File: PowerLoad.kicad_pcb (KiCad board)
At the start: 2 copper layers, 213.9 x 120 mm, 88 parts, among them IC1 L7812, J1 IN+, J2 IN-, J3 LOAD_IN+, J4 GND, J5 LOAD_IN+, U2 LM324, U3 LM324

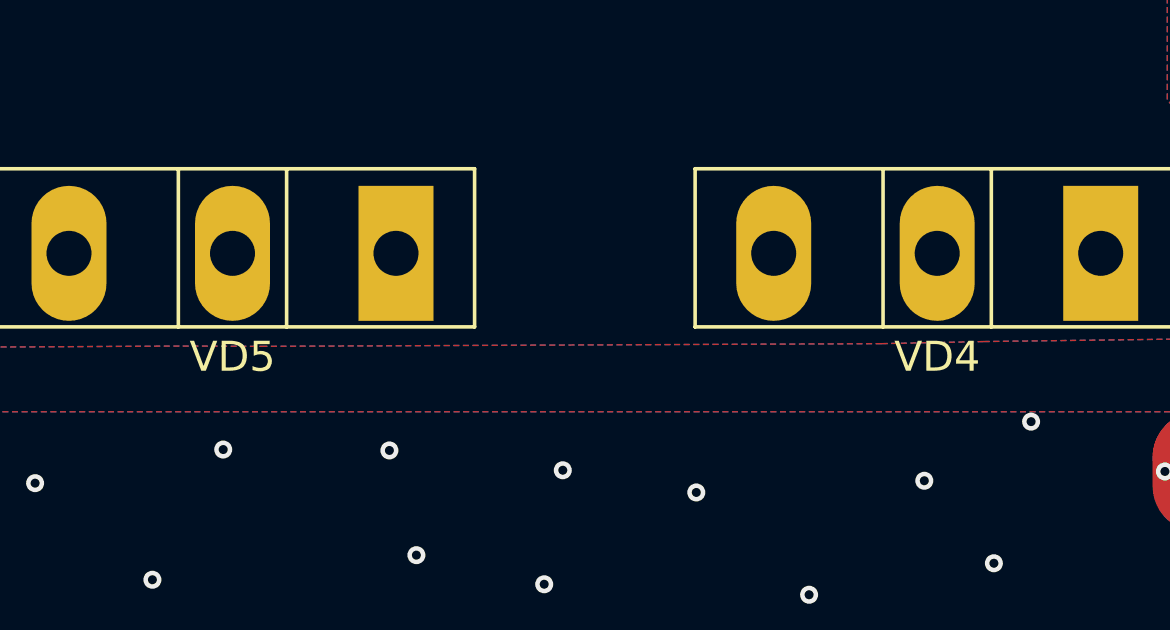
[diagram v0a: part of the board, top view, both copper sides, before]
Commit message: fixed super TO247-3
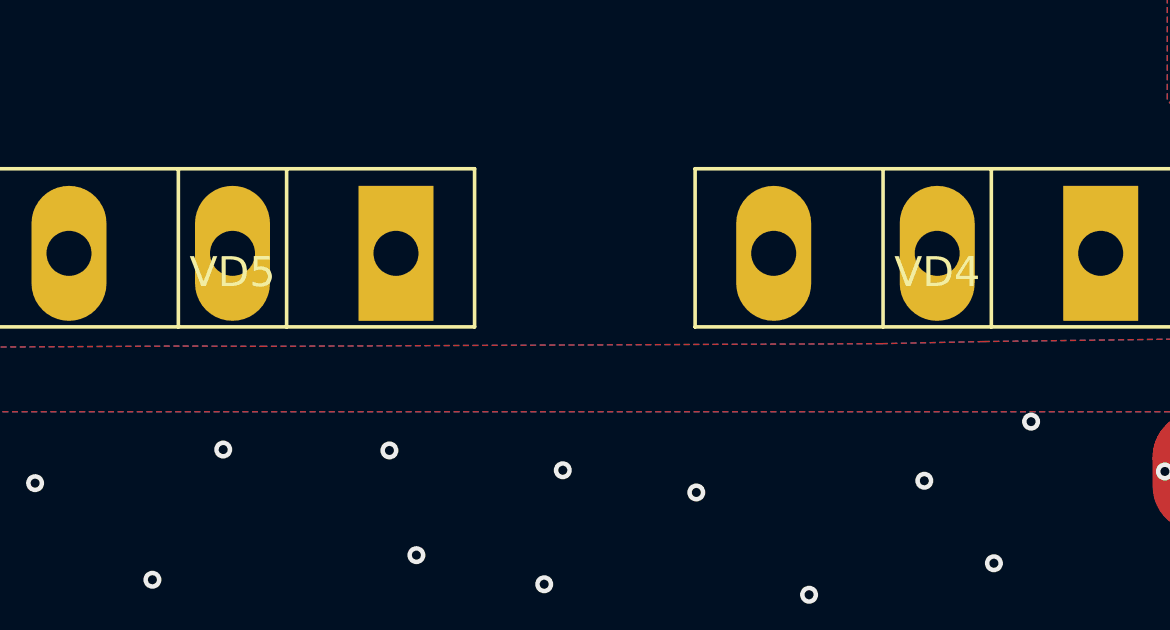
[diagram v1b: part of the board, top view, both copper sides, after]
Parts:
- VD2, VD3, VD4, VD5: footprint Package_TO_SOT_THT:TO-247-3_Vertical -> SuperTO247-3:TO-247-3(powirtab)
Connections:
- VD3 pad 2: Net-(J3-Pin_1) -> (no net)
- VD4 pad 2: Net-(J3-Pin_1) -> (no net)
- VD5 pad 2: Net-(J3-Pin_1) -> (no net)
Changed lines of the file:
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@@
 		)
 	)
-	(footprint "Package_TO_SOT_THT:TO-247-3_Vertical"
+	(footprint "SuperTO247-3:TO-247-3(powirtab)"
 		(layer "F.Cu")
 		(at 225 48.36)
@@
 		)
 		(property "Value" "80EBU02"
-			(at 5.45 3.95 0)
+			(at 5.45 6.77 0)
 			(layer "F.Fab")
 			(effects
@@
 			)
 		)
-		(pad "1" thru_hole rect
+		(pad "2" thru_hole rect
 			(at 0 0)
 			(size 2.5 4.5)
@@
 			(layers "*.Cu" "*.Mask")
 			(remove_unused_layers no)
-			(net 22 "Net-(J3-Pin_1)")
-			(pinfunction "K")
-			(pintype "passive")
 		)
 		(pad "2" thru_hole oval
@@
 			(layers "*.Cu" "*.Mask")
 			(remove_unused_layers no)
-			(net 22 "Net-(J3-Pin_1)")
-			(pinfunction "A")
-			(pintype "passive")
 		)
-		(pad "3" thru_hole oval
+		(pad "2" thru_hole oval
 			(at 10.9 0)
 			(size 2.5 4.5)
@@
 			(layers "*.Cu" "*.Mask")
 			(remove_unused_layers no)
-			(net 22 "Net-(J3-Pin_1)")
 		)
 		(embedded_fonts no)
@@
 		)
 	)
-	(footprint "Package_TO_SOT_THT:TO-247-3_Vertical"
+	(footprint "SuperTO247-3:TO-247-3(powirtab)"
 		(layer "F.Cu")
 		(at 212.41 141.31 180)
@@
 		(tags "TO-247-3 Vertical RM 5.45mm")
 		(property "Reference" "VD5"
-			(at 5.45 -3.45 0)
+			(at 5.45 -0.63 180)
 			(layer "F.SilkS")
 			(effects
@@
 		)
 		(property "Value" "80EBU02"
-			(at 5.45 3.95 0)
+			(at 5.45 6.77 180)
 			(layer "F.Fab")
 			(effects
@@
 		)
 		(property "Datasheet" ""
-			(at 0 0 0)
+			(at 0 0 180)
 			(layer "F.Fab")
 			(hide yes)
@@
 		)
 		(property "Description" "Diode, small symbol"
-			(at 0 0 0)
+			(at 0 0 180)
 			(layer "F.Fab")
 			(hide yes)
@@
 		)
 		(fp_text user "${REFERENCE}"
-			(at 5.45 -3.45 0)
+			(at 5.45 -0.63 180)
 			(layer "F.Fab")
 			(effects
@@
 			)
 		)
-		(pad "1" thru_hole rect
+		(pad "2" thru_hole rect
 			(at 0 0 180)
 			(size 2.5 4.5)
@@
 			(layers "*.Cu" "*.Mask")
 			(remove_unused_layers no)
-			(net 22 "Net-(J3-Pin_1)")
-			(pinfunction "K")
-			(pintype "passive")
 		)
 		(pad "2" thru_hole oval
@@
 			(layers "*.Cu" "*.Mask")
 			(remove_unused_layers no)
-			(net 22 "Net-(J3-Pin_1)")
-			(pinfunction "A")
-			(pintype "passive")
 		)
-		(pad "3" thru_hole oval
+		(pad "2" thru_hole oval
 			(at 10.9 0 180)
 			(size 2.5 4.5)
@@
 			(layers "*.Cu" "*.Mask")
 			(remove_unused_layers no)
-			(net 22 "Net-(J3-Pin_1)")
 		)
 		(embedded_fonts no)
@@
 		)
 	)
-	(footprint "Package_TO_SOT_THT:TO-247-3_Vertical"
+	(footprint "SuperTO247-3:TO-247-3(powirtab)"
 		(layer "F.Cu")
 		(at 201.51 48.36)
@@
 			)
 		)
-		(pad "1" thru_hole rect
+		(pad "2" thru_hole rect
 			(at 0 0)
 			(size 2.5 4.5)
@@
 			(remove_unused_layers no)
 			(net 22 "Net-(J3-Pin_1)")
-			(pinfunction "K")
+			(pinfunction "A")
 			(pintype "passive")
 		)
@@
 			(pintype "passive")
 		)
-		(pad "3" thru_hole oval
+		(pad "2" thru_hole oval
 			(at 10.9 0)
 			(size 2.5 4.5)
@@
 			(remove_unused_layers no)
 			(net 22 "Net-(J3-Pin_1)")
+			(pinfunction "A")
+			(pintype "passive")
 		)
 		(embedded_fonts no)
@@
 		)
 	)
-	(footprint "Package_TO_SOT_THT:TO-247-3_Vertical"
+	(footprint "SuperTO247-3:TO-247-3(powirtab)"
 		(layer "F.Cu")
 		(at 235.9 141.31 180)
@@
 		(tags "TO-247-3 Vertical RM 5.45mm")
 		(property "Reference" "VD4"
-			(at 5.45 -3.45 0)
+			(at 5.45 -0.63 180)
 			(layer "F.SilkS")
 			(effects
@@
 		)
 		(property "Value" "80EBU02"
-			(at 5.45 3.95 0)
+			(at 5.45 6.77 180)
 			(layer "F.Fab")
 			(effects
@@
 		)
 		(property "Datasheet" ""
-			(at 0 0 0)
+			(at 0 0 180)
 			(layer "F.Fab")
 			(hide yes)
@@
 		)
 		(property "Description" "Diode, small symbol"
-			(at 0 0 0)
+			(at 0 0 180)
 			(layer "F.Fab")
 			(hide yes)
@@
 		)
 		(fp_text user "${REFERENCE}"
-			(at 5.45 -3.45 0)
+			(at 5.45 -0.63 180)
 			(layer "F.Fab")
 			(effects
@@
 			)
 		)
-		(pad "1" thru_hole rect
+		(pad "2" thru_hole rect
 			(at 0 0 180)
 			(size 2.5 4.5)
@@
 			(layers "*.Cu" "*.Mask")
 			(remove_unused_layers no)
-			(net 22 "Net-(J3-Pin_1)")
-			(pinfunction "K")
-			(pintype "passive")
 		)
 		(pad "2" thru_hole oval
@@
 			(layers "*.Cu" "*.Mask")
 			(remove_unused_layers no)
-			(net 22 "Net-(J3-Pin_1)")
-			(pinfunction "A")
-			(pintype "passive")
 		)
-		(pad "3" thru_hole oval
+		(pad "2" thru_hole oval
 			(at 10.9 0 180)
 			(size 2.5 4.5)
@@
 			(layers "*.Cu" "*.Mask")
 			(remove_unused_layers no)
-			(net 22 "Net-(J3-Pin_1)")
 		)
 		(embedded_fonts no)
